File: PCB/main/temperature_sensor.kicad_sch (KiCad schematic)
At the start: 6 parts, among them Q3 FDS6690A, U7 MCP9700T-ETT

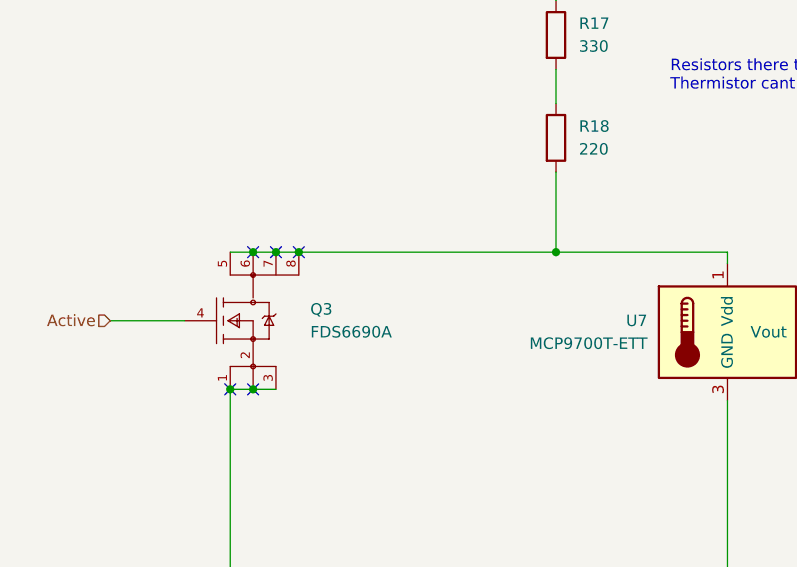
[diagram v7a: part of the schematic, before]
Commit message: Correct labels
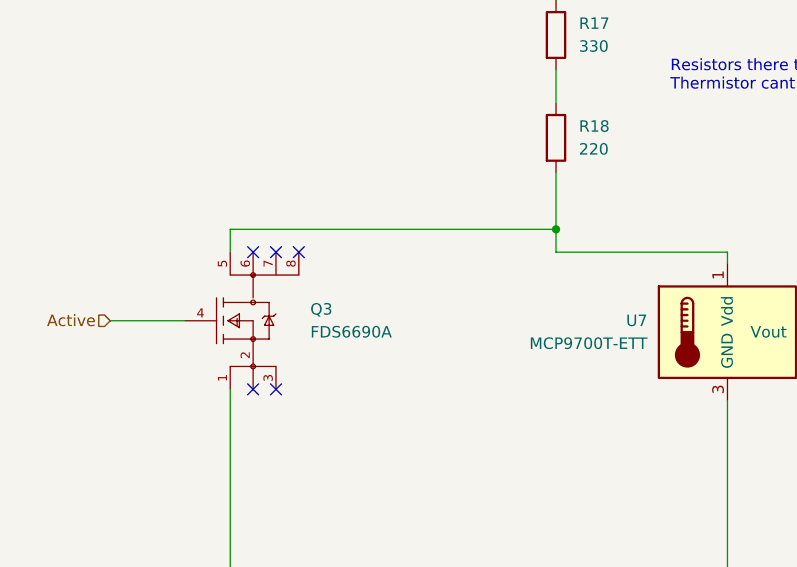
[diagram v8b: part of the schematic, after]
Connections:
- net GND: no longer Q3.2 (S), Q3.3 (S)
- net at Q3.5 (D), R18.2, U7.1 (Vdd): no longer Q3.6 (D), Q3.7 (D), Q3.8 (D)
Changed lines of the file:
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@@
     (comment 4 "Author: Kelvin Yankey")
-  )
-  (junction (at 146.05 66.04) (diameter 0) (color 0 0 0 0)
-  )
-  (junction (at 114.935 66.04) (diameter 0) (color 0 0 0 0)
-  )
-  (junction (at 112.395 81.28) (diameter 0) (color 0 0 0 0)
   )
   (junction (at 186.69 74.93) (diameter 0) (color 0 0 0 0)
@@
   (junction (at 109.855 135.89) (diameter 0) (color 0 0 0 0)
   )
-  (junction (at 112.395 66.04) (diameter 0) (color 0 0 0 0)
-  )
   (junction (at 165.1 135.89) (diameter 0) (color 0 0 0 0)
   )
-  (junction (at 109.855 81.28) (diameter 0) (color 0 0 0 0)
-  )
-  (junction (at 117.475 66.04) (diameter 0) (color 0 0 0 0)
+  (junction (at 146.05 63.5) (diameter 0) (color 0 0 0 0)
   )
   (no_connect (at 112.395 81.28))
-  (no_connect (at 109.855 81.28))
-  (no_connect (at 112.395 66.04))
   (no_connect (at 114.935 66.04))
   (no_connect (at 117.475 66.04))
+  (no_connect (at 112.395 66.04))
+  (no_connect (at 114.935 81.28))
   (wire (pts (xy 109.855 81.28) (xy 109.855 135.89))
     (stroke (width 0) (type default) (color 0 0 0 0))
@@
     (stroke (width 0) (type default) (color 0 0 0 0))
   )
-  (wire (pts (xy 117.475 66.04) (xy 146.05 66.04))
+  (wire (pts (xy 109.855 63.5) (xy 146.05 63.5))
     (stroke (width 0) (type default) (color 0 0 0 0))
   )
@@
   )
   (wire (pts (xy 146.05 35.56) (xy 146.05 38.1))
-    (stroke (width 0) (type default) (color 0 0 0 0))
-  )
-  (wire (pts (xy 114.935 66.04) (xy 117.475 66.04))
     (stroke (width 0) (type default) (color 0 0 0 0))
   )
@@
     (stroke (width 0) (type default) (color 0 0 0 0))
   )
-  (wire (pts (xy 109.855 81.28) (xy 112.395 81.28))
+  (wire (pts (xy 146.05 63.5) (xy 146.05 66.04))
     (stroke (width 0) (type default) (color 0 0 0 0))
   )
@@
     (stroke (width 0) (type default) (color 0 0 0 0))
   )
-  (wire (pts (xy 109.855 66.04) (xy 112.395 66.04))
+  (wire (pts (xy 109.855 63.5) (xy 109.855 66.04))
     (stroke (width 0) (type default) (color 0 0 0 0))
   )
-  (wire (pts (xy 146.05 57.15) (xy 146.05 66.04))
+  (wire (pts (xy 146.05 57.15) (xy 146.05 63.5))
     (stroke (width 0) (type default) (color 0 0 0 0))
   )
@@
     (stroke (width 0) (type default) (color 0 0 0 0))
   )
-  (wire (pts (xy 112.395 66.04) (xy 114.935 66.04))
-    (stroke (width 0) (type default) (color 0 0 0 0))
-  )
-  (wire (pts (xy 112.395 81.28) (xy 114.935 81.28))
-    (stroke (width 0) (type default) (color 0 0 0 0))
-  )
